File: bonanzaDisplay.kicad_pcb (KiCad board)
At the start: 6 copper layers, 61 x 101 mm, 81 parts, among them J1 OLED-1.31-SSD1322, J15 SWD, J2 Conn_01x02, J5 Conn_01x10, J6 USB_C_Receptacle_USB2.0, SW1 TS-1088-AR02016, SW2 TS-1088-AR02016, SW3 SIQ-02FVS3, U1 RP2354A, U2 XC6206P302MR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

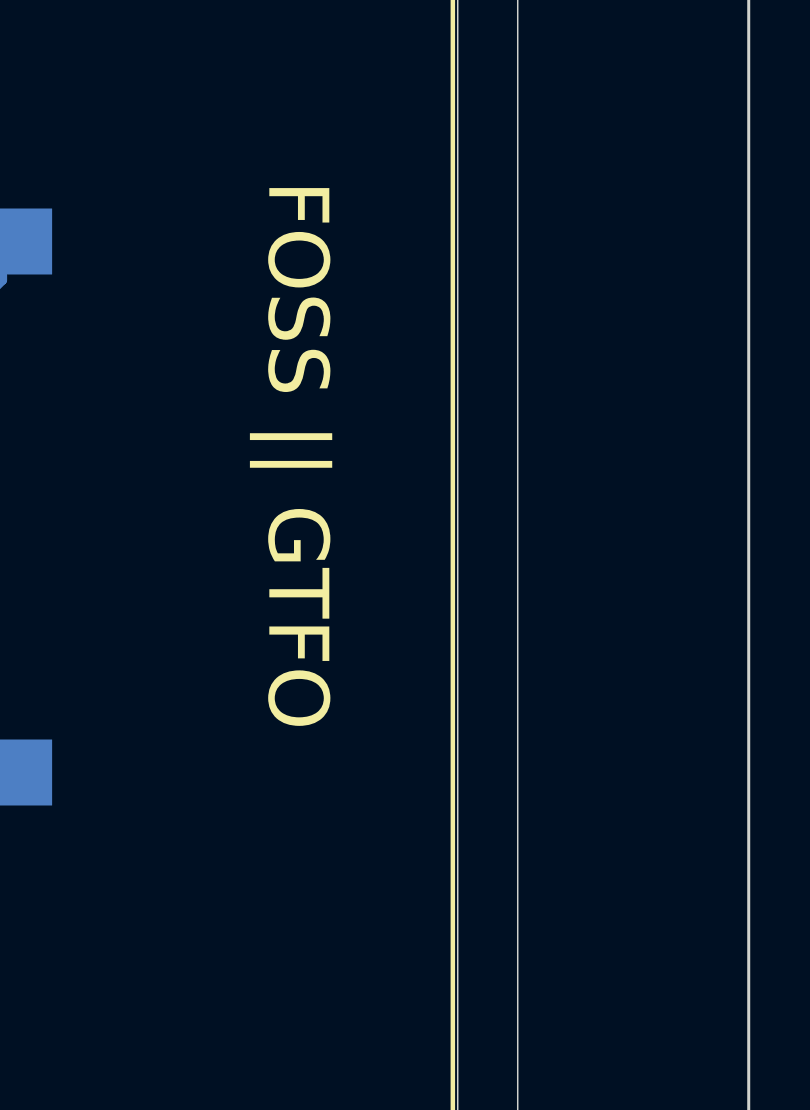
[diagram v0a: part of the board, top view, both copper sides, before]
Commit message: updated BOM with some cheaper JLC Basic parts
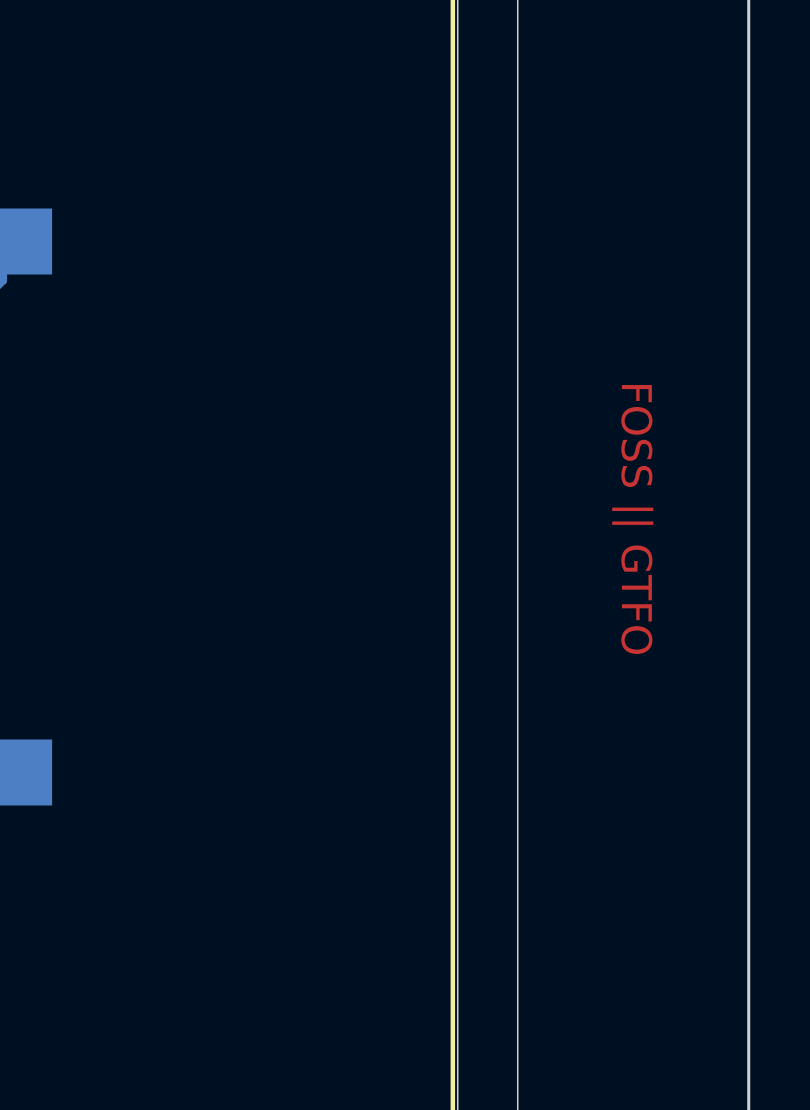
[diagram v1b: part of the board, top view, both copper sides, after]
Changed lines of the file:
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@@
 		(embedded_fonts no)
 		(model "${KICAD10_3DMODEL_DIR}/Connector_PinHeader_2.54mm.3dshapes/PinHeader_1x02_P2.54mm_Vertical.step"
+			(hide yes)
 			(offset
 				(xyz 0 0 0)
@@
 		(layer "Edge.Cuts")
 	)
+	(gr_text "FOSS || GTFO"
+		(at 156.65 85.3 270)
+		(layer "F.Cu")
+		(effects
+			(font
+				(size 1 1)
+				(thickness 0.15)
+			)
+			(justify left bottom)
+		)
+	)
 	(gr_text "SWD"
 		(at 104.565 120.45 0)
@@
 			)
 			(justify left bottom)
-		)
-	)
-	(gr_text "FOSS || GTFO"
-		(at 144.775 78.6 270)
-		(layer "F.SilkS")
-		(effects
-			(font
-				(size 2 2)
-				(thickness 0.3)
-			)
-			(justify left bottom)
